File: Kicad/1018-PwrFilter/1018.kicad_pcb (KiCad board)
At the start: 2 copper layers, 50 x 100 mm, 30 parts, among them P1 CONN2X3MOLEX, P10 CONN_6, P11 TST, P12 TST, P13 TST, P14 TST, P15 TST, P16 TST, P4 TST, P7 TST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

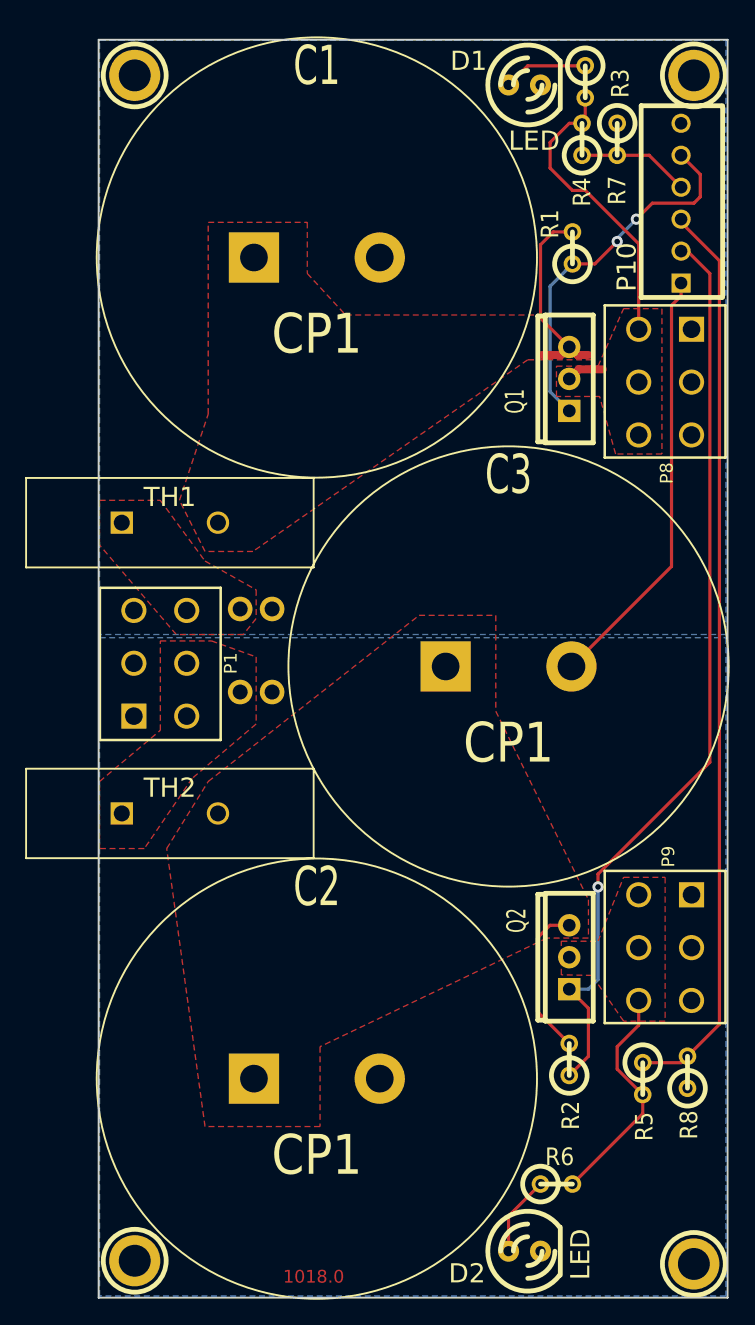
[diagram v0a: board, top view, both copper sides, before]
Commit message: Kicad updates: Added IncandWing (1014.zip), PwrFilter (1018.zip), updated Sol Panel (Panel-1013.zip), Incand Panel (Panel-1014.zip), and Pwr Filter Panel (Panel-1018.zip).  Panels had a different drill origin than PCB origin.
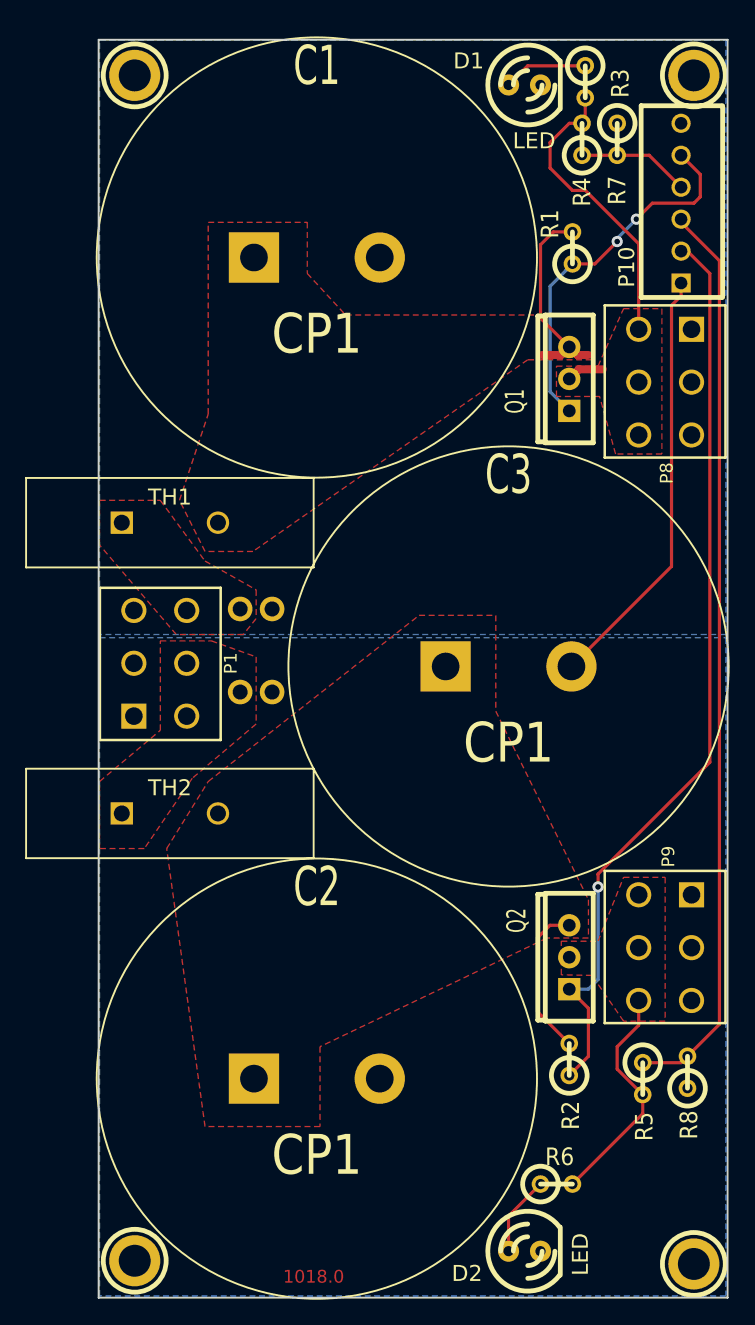
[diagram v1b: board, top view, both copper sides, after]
